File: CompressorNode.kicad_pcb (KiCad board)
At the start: 2 copper layers, 127 x 80 mm, 33 parts, among them J1 EXT1, J10 Screw_Terminal_01x03, J11 Screw_Terminal_01x02, J12 Screw_Terminal_01x03, J13 Screw_Terminal_01x04, J2 Screw_Terminal_01x04, J3 Screw_Terminal_01x03, J4 EXT2, J5 Screw_Terminal_01x02, J6 Screw_Terminal_01x02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

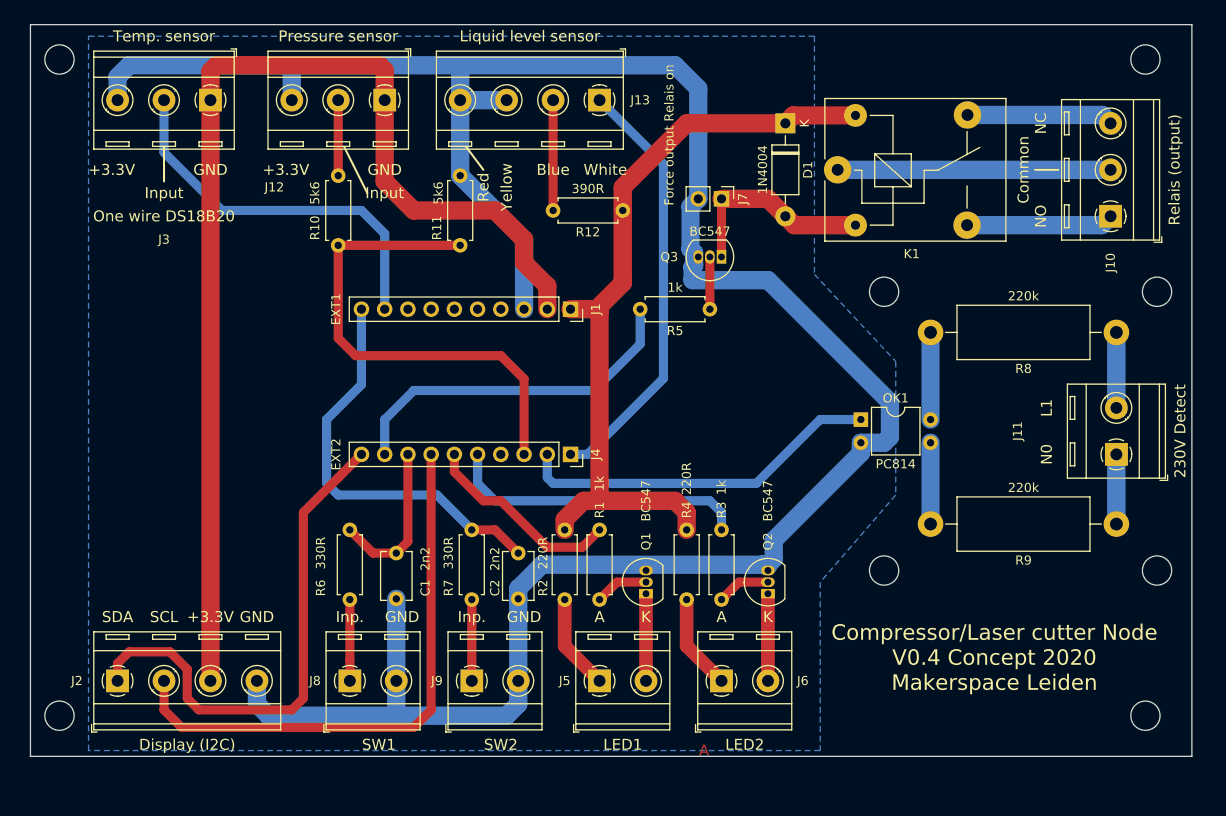
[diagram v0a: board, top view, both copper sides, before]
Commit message: corrected the groundplane and som PCB lines to create more distance to the 230V components
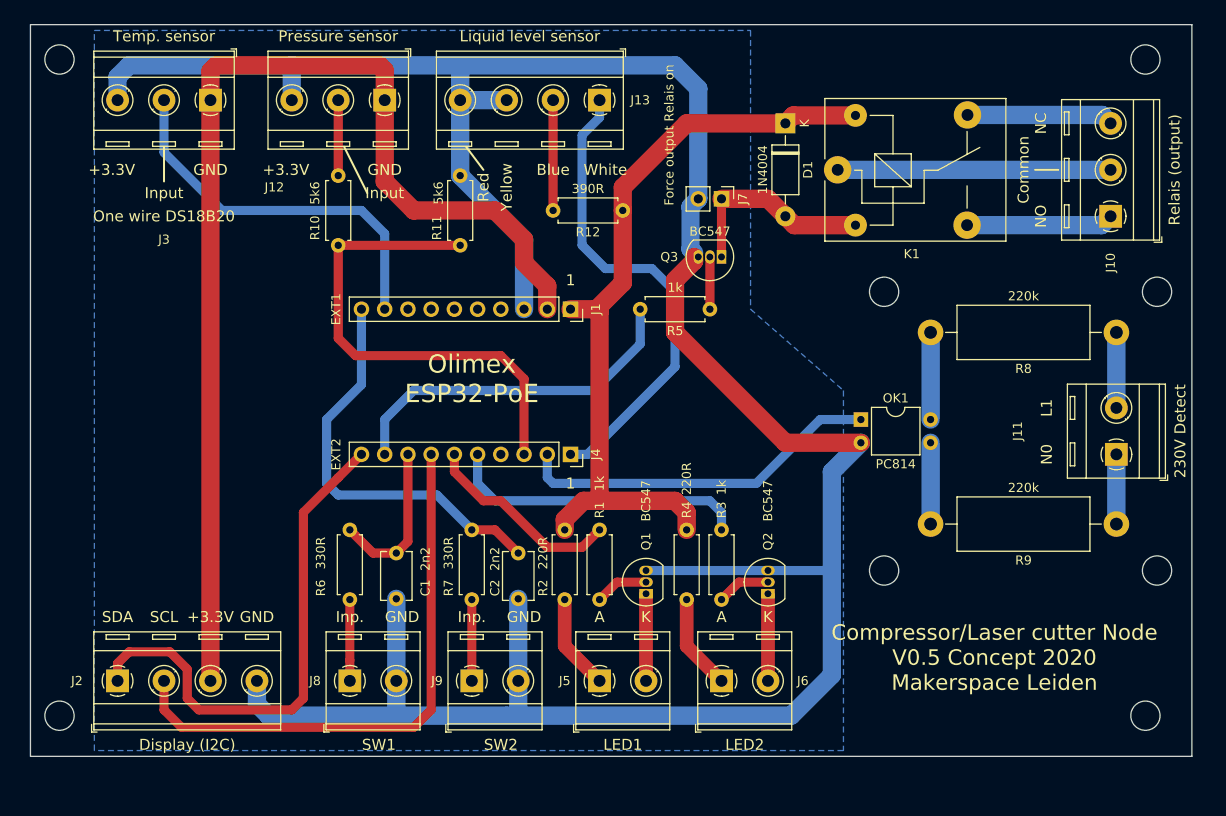
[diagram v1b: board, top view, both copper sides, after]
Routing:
- net GND: track 266.2 -> 299.4 mm
- net GPI39: track 46.9 -> 52.5 mm
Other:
- board text added: "1"
- board text added: "Compressor/Laser cutter Node V0.5 Concept 2020 Makerspace Leiden"
- board text added: "Olimex ESP32-PoE"
- board text removed: "Compressor/Laser cutter Node V0.4 Concept 2020 Makerspace Leiden"
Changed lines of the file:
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@@
   (general
     (thickness 1.6)
-    (drawings 56)
+    (drawings 58)
     (tracks 165)
     (zones 0)
@@
   (title_block
     (title CompressorNode)
-    (date 2020-03-25)
-    (rev "V0.4 Concept")
+    (date 2020-03-27)
+    (rev "V0.5 Concept")
     (company "MakerSpace Leiden")
     (comment 1 "Getekend door Hans Beerman")
@@
   )
   (setup
-    (last_trace_width 0.25)
+    (last_trace_width 1)
     (user_trace_width 0.5)
     (user_trace_width 0.75)
@@
     )
   )
+  (gr_text 1 (at 144.145 83.185) (layer F.SilkS)
+    (effects (font (size 1.2 1.2) (thickness 0.3)))
+  )
+  (gr_text 1 (at 144.145 105.41) (layer F.SilkS)
+    (effects (font (size 1.2 1.2) (thickness 0.3)))
+  )
+  (gr_text "Olimex\nESP32-PoE" (at 133.35 93.98) (layer F.SilkS)
+    (effects (font (size 2 2) (thickness 0.3)))
+  )
   (gr_line (start 99.695 72.39) (end 99.695 68.58) (layer F.SilkS) (width 0.22))
   (gr_text L1 (at 196.215 97.155 90) (layer F.SilkS)
@@
     (effects (font (size 1.2 1.2) (thickness 0.3)))
   )
-  (gr_text "Compressor/Laser cutter Node\nV0.4 Concept 2020\nMakerspace Leiden" (at 190.5 124.46) (layer F.SilkS)
+  (gr_text "Compressor/Laser cutter Node\nV0.5 Concept 2020\nMakerspace Leiden" (at 190.5 124.46) (layer F.SilkS)
     (effects (font (size 1.7 1.7) (thickness 0.3)))
   )
@@
   )
   (gr_text A (at 160.655 120.015) (layer F.SilkS)
-    (effects (font (size 1.2 1.2) (thickness 0.3)))
-  )
-  (gr_text A (at 158.75 134.62) (layer F.Cu)
     (effects (font (size 1.2 1.2) (thickness 0.3)))
   )
@@
   (segment (start 158.115 62.23) (end 158.115 74.295) (width 2) (layer B.Cu) (net 1))
   (segment (start 155.575 59.69) (end 158.115 62.23) (width 2) (layer B.Cu) (net 1))
-  (segment (start 141.02863 114.3) (end 165.1 114.3) (width 2) (layer B.Cu) (net 1))
-  (segment (start 138.43 116.89863) (end 141.02863 114.3) (width 2) (layer B.Cu) (net 1))
-  (segment (start 138.43 118.03) (end 138.43 116.89863) (width 2) (layer B.Cu) (net 1))
-  (segment (start 165.1 114.3) (end 165.735 114.47999) (width 2) (layer B.Cu) (net 1))
-  (segment (start 165.735 114.3) (end 165.1 114.3) (width 2) (layer B.Cu) (net 1))
-  (segment (start 166.37 113.665) (end 165.735 114.3) (width 2) (layer B.Cu) (net 1))
-  (segment (start 166.37 111.62137) (end 166.37 113.665) (width 2) (layer B.Cu) (net 1))
-  (segment (start 175.895 100.965) (end 175.895 102.09637) (width 2) (layer B.Cu) (net 1))
-  (segment (start 175.895 102.09637) (end 166.37 111.62137) (width 2) (layer B.Cu) (net 1))
-  (segment (start 138.43 118.03) (end 138.43 127) (width 2) (layer B.Cu) (net 1))
-  (segment (start 138.43 129.54) (end 138.43 127) (width 2) (layer B.Cu) (net 1))
-  (segment (start 137.16 130.81) (end 138.43 129.54) (width 2) (layer B.Cu) (net 1))
   (segment (start 125.095 127) (end 125.095 130.81) (width 2) (layer B.Cu) (net 1))
   (segment (start 125.095 130.81) (end 137.16 130.81) (width 2) (layer B.Cu) (net 1))
@@
   (segment (start 157.265001 79.795001) (end 157.265001 75.144999) (width 2) (layer B.Cu) (net 1))
   (segment (start 157.65999 80.18999) (end 157.265001 79.795001) (width 2) (layer B.Cu) (net 1))
-  (segment (start 157.65999 81.584522) (end 157.65999 80.18999) (width 2) (layer B.Cu) (net 1))
-  (segment (start 178.435 100.965) (end 179.07 100.33) (width 2) (layer B.Cu) (net 1))
-  (segment (start 175.895 100.965) (end 178.435 100.965) (width 2) (layer B.Cu) (net 1))
-  (segment (start 179.07 100.33) (end 179.07 96.52) (width 2) (layer B.Cu) (net 1))
-  (segment (start 157.48 81.764512) (end 157.65999 81.584522) (width 2) (layer B.Cu) (net 1))
-  (segment (start 179.07 96.52) (end 165.735 83.185) (width 2) (layer B.Cu) (net 1))
-  (segment (start 165.735 83.185) (end 157.48 83.185) (width 2) (layer B.Cu) (net 1))
   (segment (start 157.265001 75.144999) (end 158.115 74.295) (width 2) (layer B.Cu) (net 1))
-  (segment (start 157.48 83.185) (end 157.48 81.764512) (width 2) (layer B.Cu) (net 1))
+  (segment (start 157.65999 81.10001) (end 157.65999 80.645) (width 2) (layer F.Cu) (net 1))
+  (segment (start 155.575 83.185) (end 157.65999 81.10001) (width 2) (layer F.Cu) (net 1))
+  (segment (start 155.575 88.9) (end 155.575 83.185) (width 2) (layer F.Cu) (net 1))
+  (segment (start 175.895 100.965) (end 167.64 100.965) (width 2) (layer F.Cu) (net 1))
+  (segment (start 167.64 100.965) (end 155.575 88.9) (width 2) (layer F.Cu) (net 1))
+  (segment (start 138.43 127) (end 138.43 118.03) (width 2) (layer B.Cu) (net 1))
+  (segment (start 168.275 130.81) (end 172.72 126.365) (width 2) (layer B.Cu) (net 1))
+  (segment (start 172.72 104.14) (end 175.895 100.965) (width 2) (layer B.Cu) (net 1))
+  (segment (start 138.43 127) (end 138.43 130.81) (width 2) (layer B.Cu) (net 1))
+  (segment (start 137.16 130.81) (end 138.43 130.81) (width 2) (layer B.Cu) (net 1))
+  (segment (start 138.43 130.81) (end 168.275 130.81) (width 2) (layer B.Cu) (net 1))
+  (segment (start 154.15 114.935) (end 172.72 114.935) (width 1) (layer B.Cu) (net 1))
+  (segment (start 152.4 114.935) (end 154.15 114.935) (width 1) (layer B.Cu) (net 1))
+  (segment (start 172.72 126.365) (end 172.72 114.935) (width 2) (layer B.Cu) (net 1))
+  (segment (start 172.72 114.935) (end 172.72 104.14) (width 2) (layer B.Cu) (net 1))
   (segment (start 126.365 111.76) (end 125.095 113.03) (width 1) (layer F.Cu) (net 2))
   (segment (start 126.365 102.235) (end 126.365 111.76) (width 1) (layer F.Cu) (net 2))
@@
   (segment (start 141.605 104.775) (end 142.24 105.41) (width 1) (layer B.Cu) (net 14))
   (segment (start 145.995 102.235) (end 144.145 102.235) (width 1) (layer B.Cu) (net 15))
-  (segment (start 154.305 93.925) (end 145.995 102.235) (width 1) (layer B.Cu) (net 15))
-  (segment (start 147.32 63.5) (end 154.305 70.485) (width 1) (layer B.Cu) (net 15))
-  (segment (start 154.305 70.485) (end 154.305 93.925) (width 1) (layer B.Cu) (net 15))
+  (segment (start 155.575 92.655) (end 145.995 102.235) (width 1) (layer B.Cu) (net 15))
+  (segment (start 155.575 84.455) (end 155.575 92.655) (width 1) (layer B.Cu) (net 15))
+  (segment (start 147.32 65.405) (end 145.415 67.31) (width 1) (layer B.Cu) (net 15))
+  (segment (start 145.415 79.375) (end 147.955 81.915) (width 1) (layer B.Cu) (net 15))
+  (segment (start 147.955 81.915) (end 153.035 81.915) (width 1) (layer B.Cu) (net 15))
+  (segment (start 147.32 63.5) (end 147.32 65.405) (width 1) (layer B.Cu) (net 15))
+  (segment (start 153.035 81.915) (end 155.575 84.455) (width 1) (layer B.Cu) (net 15))
+  (segment (start 145.415 67.31) (end 145.415 79.375) (width 1) (layer B.Cu) (net 15))
   (segment (start 152.4 127) (end 152.4 117.68001) (width 1.5) (layer F.Cu) (net 16))
   (segment (start 143.51 123.19) (end 147.32 127) (width 1.5) (layer F.Cu) (net 17))
@@
     (polygon
       (pts
-        (xy 170.815 82.55) (xy 179.705 92.075) (xy 179.705 106.68) (xy 171.45 116.205) (xy 171.45 134.62)
-        (xy 91.44 134.62) (xy 91.44 56.515) (xy 170.815 56.515)
+        (xy 163.83 86.36) (xy 173.99 95.25) (xy 173.99 134.62) (xy 92.075 134.62) (xy 92.075 55.88)
+        (xy 163.83 55.88)
       )
     )

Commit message: corrected the distance between the two connectors for the ESP32-PoE
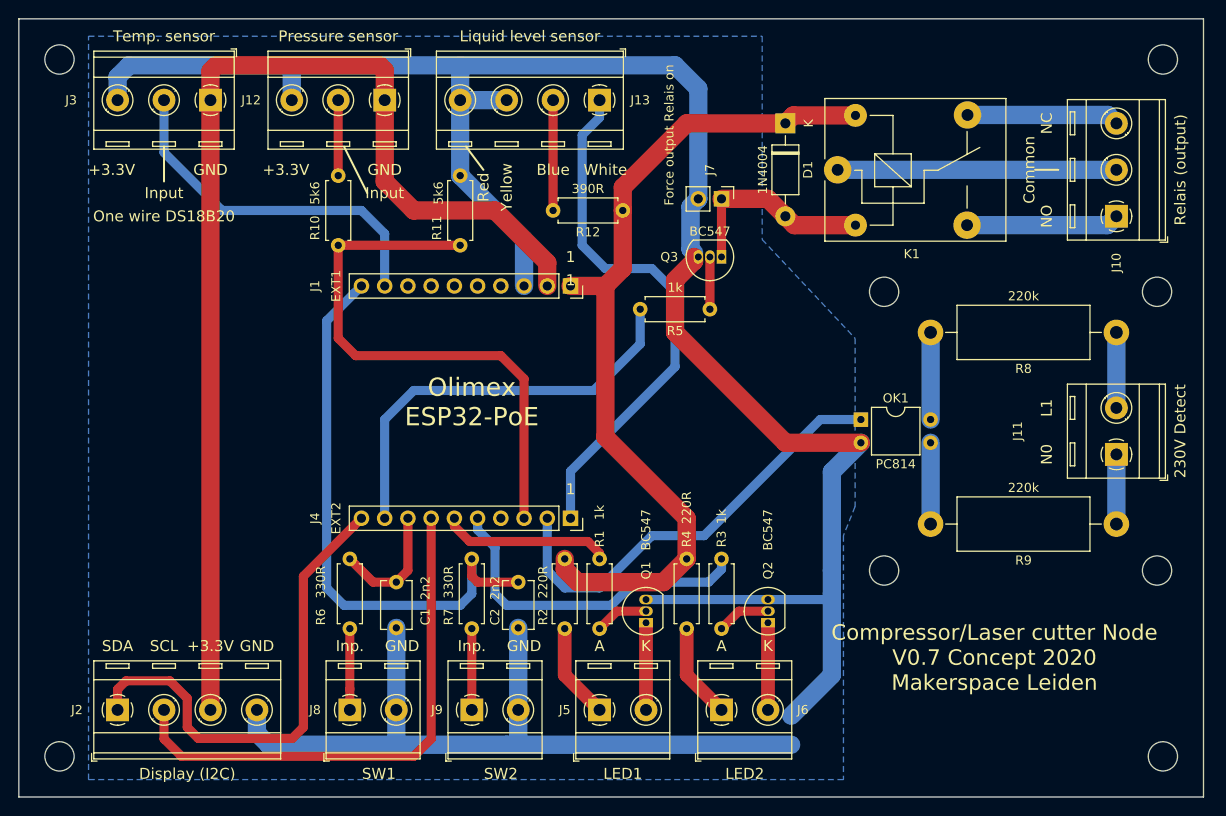
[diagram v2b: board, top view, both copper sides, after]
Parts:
- moved J4 6.98 mm to (144.1, 109.2)
- moved J2 3.18 mm to (94.6, 130.2)
- moved J5 3.18 mm to (147.3, 130.2)
- moved J6 3.18 mm to (160.7, 130.2)
- moved J8 3.18 mm to (120.0, 130.2)
- moved J9 3.18 mm to (133.3, 130.2)
- moved Q1 3.18 mm to (152.4, 120.7)
- moved Q2 3.18 mm to (165.7, 120.7)
- moved R2 3.18 mm to (143.5, 113.7)
- moved R4 3.18 mm to (156.8, 113.7)
- moved C1 3.17 mm to (125.1, 116.2)
- moved C2 3.17 mm to (138.4, 116.2)
- moved R1 3.17 mm to (147.3, 121.3)
- moved R3 3.17 mm to (160.7, 121.3)
- moved R6 3.17 mm to (120.0, 121.3)
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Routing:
- net GPIO5_SPI_C5: track 44.7 -> 62.8 mm
- net +5V: track 84.9 -> 93.7 mm
- net GPI36_U1RXD: track 40.0 -> 48.4 mm
- net GPIO14_HS2_CLK: track 39.0 -> 46.0 mm
- net GPI35: track 53.9 -> 60.9 mm
- net GPI39: track 52.5 -> 58.4 mm
- net GPIO33: track 33.1 -> 37.1 mm
- net GPIO16_I2C-SCL: track 61.9 -> 58.1 mm
- net GPIO15_HS2_CMD: track 17.5 -> 13.6 mm
- net GPIO13_I2C-SDA: track 57.1 -> 53.4 mm
- net GPIO32: track 22.0 -> 18.6 mm
- net GPIO4_U1TXD: track 41.8 -> 39.2 mm
- net GND: track 299.4 -> 297.1 mm
- net Net-(J10-Pad2): track 29.8 -> 30.5 mm
- net Net-(J10-Pad1): track 16.1 -> 16.7 mm
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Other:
- board size 127 x 80 mm -> 129.5 x 85.1 mm
- board text added: "Compressor/Laser cutter Node V0.7 Concept 2020 Makerspace Leiden"
- board text removed: "Compressor/Laser cutter Node V0.5 Concept 2020 Makerspace Leiden"
